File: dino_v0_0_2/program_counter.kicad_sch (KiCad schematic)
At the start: 18 parts, among them U1 74LS193, U10 74LS04, U11 74LS245, U12 74LS245, U13 74LS245, U14 74LS245, U2 74LS193, U3 74LS193, U4 74LS193

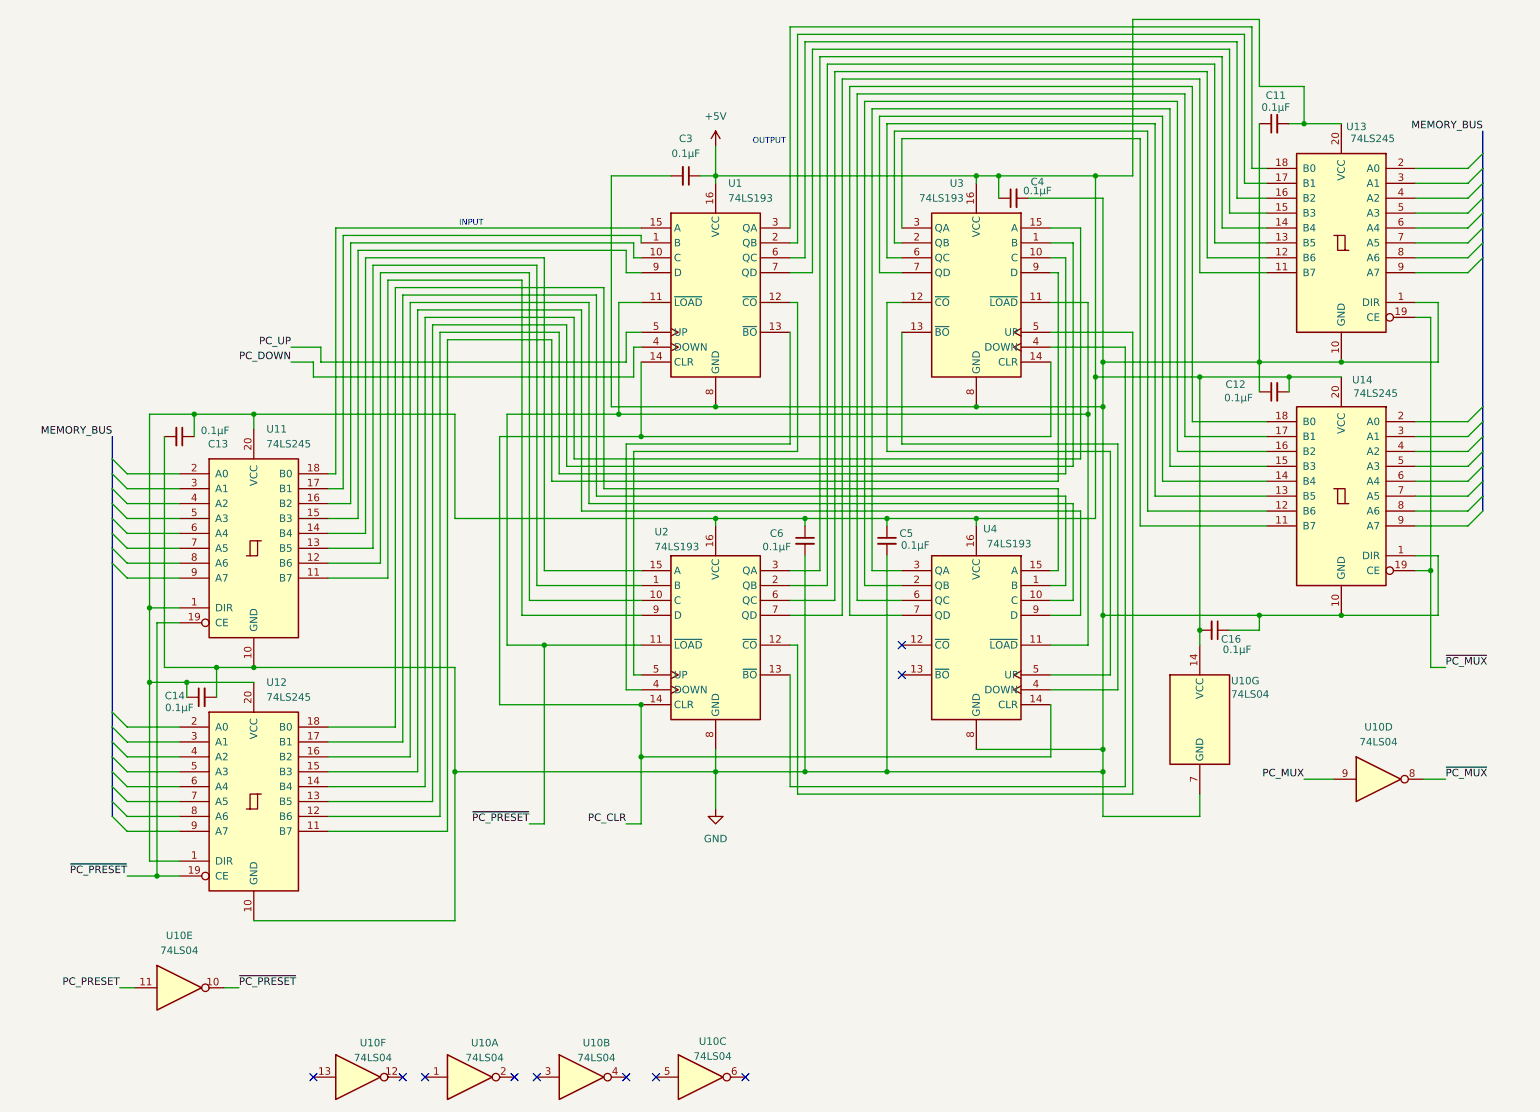
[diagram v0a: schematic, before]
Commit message: DINO v0.0.3: complete ALU/control-word, add MAR+reset sheets, wire reset circuit
ALU sheet: flags register moved from '173 (not in stock) to '273 + a '157
mux to emulate the missing load-enable pins; Z-detect built from a NOR+AND
De Morgan tree instead of a '260; ALU_CIN built from NAND(SA1,SA0) reusing
two already-placed spare gates instead of a dedicated XOR/'86. Sheet is
now fully wired and netlist-clean.

Control word sheet: all 16 CW bits assigned and wired (3x '138 decoders
for the load/source/misc fields, direct bus taps for HALT/PC_MAR_MUX/
PC_UP/END and the ALU SA[2:0] select). Found and fixed several cross-
sheet signal-name mismatches this uncovered (OUT_REG_LOAD/REG_OUT_LOAD,
PC_MAR_MUX/PC_MUX, T-state counter labels, a mirror-reversed IRB->ROM-
address buffer in microcode).

New: MAR and reset sheets, wired into the root hierarchy. Reset circuit
is a from-scratch design: RC+button+74HC14 Schmitt front end feeds the
async PRESET of the clock cluster's spare '74 half (U27B), synchronizing
release to CLK; its Q/~Q fan out to the flags register, the T-state
counter's clear, and (OR'd with the existing microcode-driven PC_CLEAR,
reusing spare gates on the same '02) the PC counters' clear.

Deprecated 7 schematic files no longer referenced by the root sheet's
hierarchy into dino_v0_0_2/deprecated/. Added docs/notes/kicad_netlist.py,
a .kicad_sch connectivity auditor (pin/net resolution incl. buses and
same-name local-label merging) used throughout this session to find the
above bugs; archived completed-work docs into docs/notes/Done/ and
rewrote dino_session_state.md as the current authoritative state+TODO.

Co-Authored-By: Claude Sonnet 5 <noreply@anthropic.com>
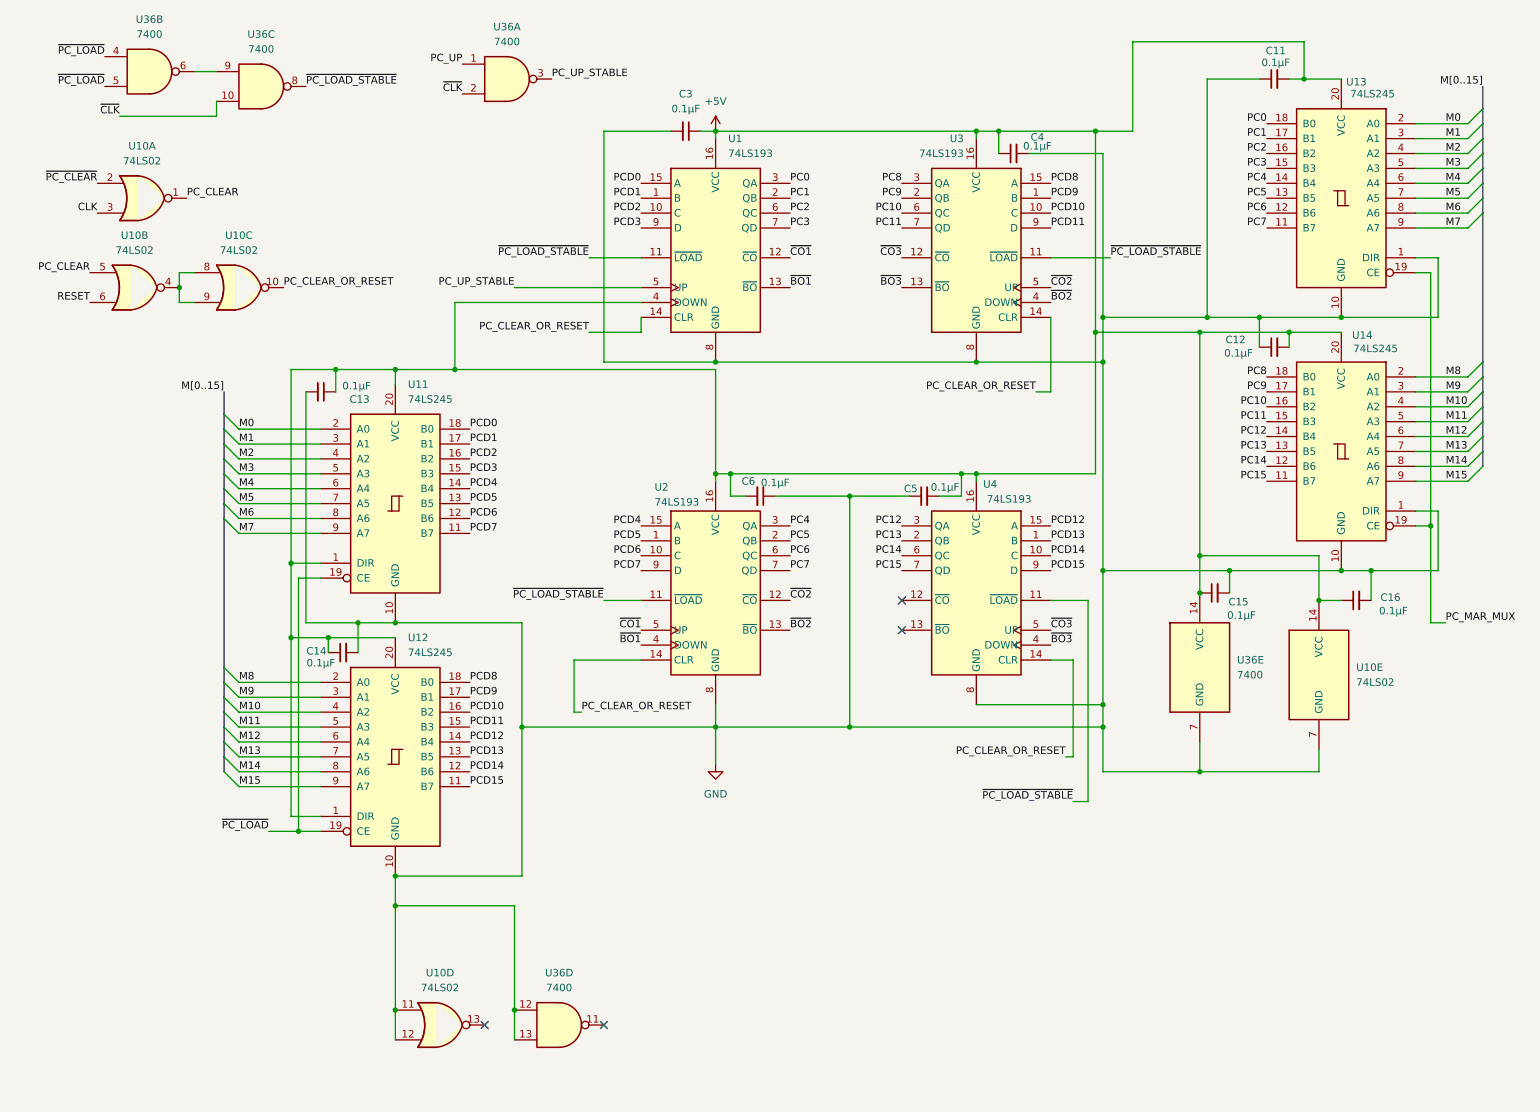
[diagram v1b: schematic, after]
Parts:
- removed U10: 74LS04, symbol 74xx:74LS04
- added C15: 0.1µF, symbol Device:C_Small
- added U10: 74LS02, symbol 74xx:74LS02
- added U36: 7400, symbol 74xx:7400
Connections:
- net PC_DOWN is gone; now on net +5V: U1.4 (DOWN)
- net +5V: now also C16.1, C5.2, C6.2, C15.1, U10.14 (VCC), U36.14 (VCC); no longer C16.2, C5.1, C6.1
- net GND: now also C16.2, C5.1, C6.1, C15.2, U10.11, U10.12, U10.7 (GND), U36.12, U36.13, U36.7 (GND); no longer C16.1, C5.2, C6.2
- net PC_UP: now also U36.1; no longer U1.5 (UP)
- net PCD13: now reaches U12.13 (B5)
- net PCD13: now also U4.1 (B); no longer U3.1 (B)
- net PCD10: now reaches U3.10 (C)
- net PCD10: now also U12.16 (B2); no longer U12.12 (B6)
- net ~{CO3}: now reaches U3.12 (~{CO}), U4.5 (UP)
- net ~{BO3}: now reaches U3.13 (~{BO}), U4.4 (DOWN)
- net PCD12: now reaches U12.14 (B4)
- net PCD12: now also U4.15 (A); no longer U3.15 (A)
- net PC14: now reaches U14.12 (B6)
- net PC14: now also U4.6 (QC); no longer U3.2 (QB)
- net PC15: now reaches U14.11 (B7)
- net PC15: now also U4.7 (QD); no longer U3.3 (QA)
- net ~{BO2}: now reaches U2.13 (~{BO}), U3.4 (DOWN)
- net ~{CO2}: now reaches U2.12 (~{CO}), U3.5 (UP)
- net PC10: now reaches U3.6 (QC)
- net PC10: now also U14.16 (B2); no longer U14.13 (B5)
- net PC11: now reaches U3.7 (QD)
- net PC11: now also U14.15 (B3); no longer U14.14 (B4)
- net PCD11: now reaches U3.9 (D)
- net PCD11: now also U12.15 (B3); no longer U12.11 (B7)
- net PC12: now reaches U4.3 (QA)
- net PC12: now also U14.14 (B4); no longer U14.15 (B3)
- net PC13: now reaches U4.2 (QB)
- net PC13: now also U14.13 (B5); no longer U14.16 (B2)
- net PC9: now reaches U14.17 (B1)
- net PC9: now also U3.2 (QB); no longer U4.6 (QC)
- net PC8: now reaches U14.18 (B0)
- net PC8: now also U3.3 (QA); no longer U4.7 (QD)
- net M8: now reaches U14.2 (A0)
- net M8: now also U12.2 (A0)
- net M9: now reaches U14.3 (A1)
- net M9: now also U12.3 (A1)
- net M10: now reaches U14.4 (A2)
- net M10: now also U12.4 (A2)
- net M11: now reaches U14.5 (A3)
- net M11: now also U12.5 (A3)
- net M12: now reaches U14.6 (A4)
- net M12: now also U12.6 (A4)
- net M13: now reaches U14.7 (A5)
- net M13: now also U12.7 (A5)
- net M14: now reaches U14.8 (A6)
- net M14: now also U12.8 (A6)
- net M15: now reaches U14.9 (A7)
- net M15: now also U12.9 (A7)
- net PCD15: now reaches U4.9 (D)
- net PCD15: now also U12.11 (B7); no longer U12.15 (B3)
- net PCD14: now reaches U4.10 (C)
- net PCD14: now also U12.12 (B6); no longer U12.16 (B2)
- net PCD9: now reaches U12.17 (B1)
- net PCD9: now also U3.1 (B); no longer U4.1 (B)
- net PCD8: now reaches U12.18 (B0)
- net PCD8: now also U3.15 (A); no longer U4.15 (A)
- net PCD7: now reaches U11.11 (B7), U2.9 (D)
- net PCD6: now reaches U11.12 (B6), U2.10 (C)
- net PCD5: now reaches U11.13 (B5), U2.1 (B)
- net PCD4: now reaches U11.14 (B4), U2.15 (A)
- net PCD3: now reaches U1.9 (D), U11.15 (B3)
- net PCD2: now reaches U1.10 (C), U11.16 (B2)
- net PCD1: now reaches U1.1 (B), U11.17 (B1)
- net PCD0: now reaches U1.15 (A), U11.18 (B0)
- net M0: now reaches U11.2 (A0)
- net M0: now also U13.2 (A0)
- net M1: now reaches U11.3 (A1)
- net M1: now also U13.3 (A1)
- net M2: now reaches U11.4 (A2)
- net M2: now also U13.4 (A2)
- net M3: now reaches U11.5 (A3)
- net M3: now also U13.5 (A3)
- net M4: now reaches U11.6 (A4)
- net M4: now also U13.6 (A4)
- net M5: now reaches U11.7 (A5)
- net M5: now also U13.7 (A5)
- net M6: now reaches U11.8 (A6)
- net M6: now also U13.8 (A6)
- net M7: now reaches U11.9 (A7)
- net M7: now also U13.9 (A7)
- net ~{CO1}: now reaches U1.12 (~{CO}), U2.5 (UP)
- net ~{BO1}: now reaches U1.13 (~{BO}), U2.4 (DOWN)
- net PC1: now reaches U1.2 (QB), U13.17 (B1)
- net PC0: now reaches U1.3 (QA), U13.18 (B0)
- net PC2: now reaches U1.6 (QC), U13.16 (B2)
- net PC3: now reaches U1.7 (QD), U13.15 (B3)
- net PC5: now reaches U13.13 (B5), U2.2 (QB)
- net PC4: now reaches U13.14 (B4), U2.3 (QA)
- net PC6: now reaches U13.12 (B6), U2.6 (QC)
- net PC7: now reaches U13.11 (B7), U2.7 (QD)
- net PC_CLR renamed PC_CLEAR_OR_RESET
- net PC_CLEAR_OR_RESET: now also U10.10
- net ~{PC_MUX} renamed PC_MAR_MUX
- net ~{PC_PRESET} renamed ~{PC_LOAD_STABLE}
- net ~{PC_LOAD_STABLE}: now also U36.8; no longer U11.19 (CE), U12.19 (CE)
- new net: U36.6, U36.9
- new net: U10.4, U10.8, U10.9
- new net CLK: U10.3
- new net PC_CLEAR: U10.1, U10.5
- new net PC_UP_STABLE: U1.5 (UP), U36.3
- new net RESET: U10.6
- new net ~{CLK}: U36.10, U36.2
- new net ~{PC_CLEAR}: U10.2
- new net ~{PC_LOAD}: U11.19 (CE), U12.19 (CE), U36.4, U36.5
- no-connect marks 10 -> 4
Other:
- note removed: "INPUT"
- note removed: "OUTPUT"
- moved on the sheet: C11, C12, C13, C14, C3, C4, C5, C6, U1, U11, U12, U13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
